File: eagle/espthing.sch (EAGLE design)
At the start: 15 parts, among them IC2 LM1117-3.3, U1 MAX3232

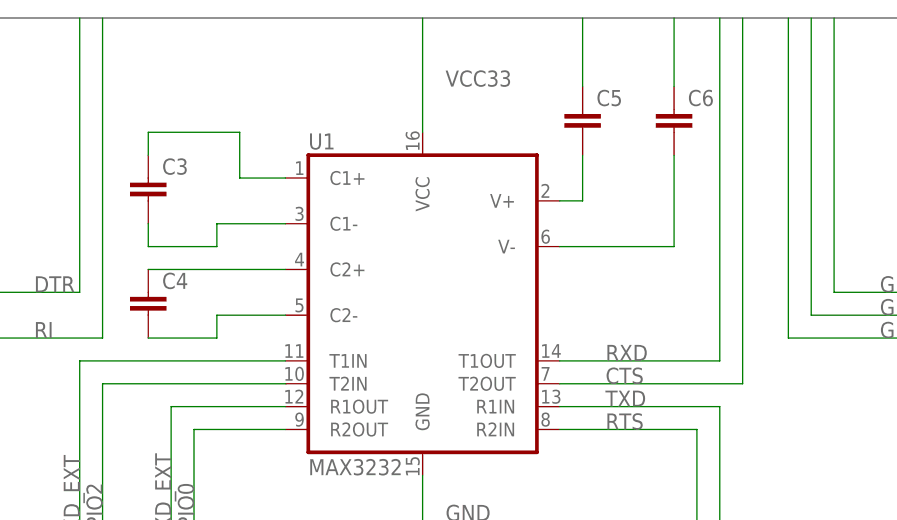
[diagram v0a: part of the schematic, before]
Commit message: added bom
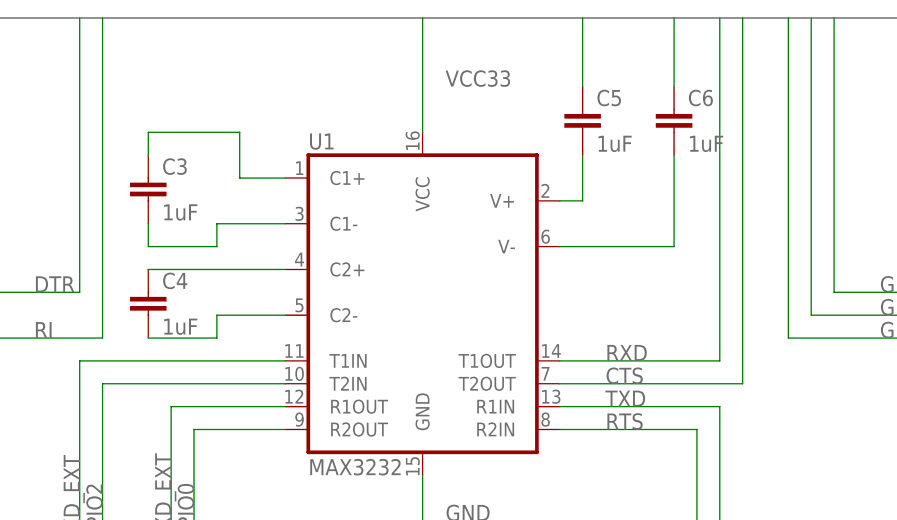
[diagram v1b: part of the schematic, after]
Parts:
- C3, C4, C5, C6: value (none) -> 1uF
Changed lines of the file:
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@@
 <part name="12VPWR" library="SparkFun-Retired" deviceset="JUMPER-2" device="PTH" value="EXT12v"/>
 <part name="X1" library="SparkFun-Retired" library_urn="urn:adsk.eagle:library:533" deviceset="DB25_FEMALE" device="HP" package3d_urn="urn:adsk.eagle:package:41386042/1"/>
-<part name="C3" library="rcl" library_urn="urn:adsk.eagle:library:334" deviceset="C-EU" device="C1206" package3d_urn="urn:adsk.eagle:package:23618/2"/>
-<part name="C4" library="rcl" library_urn="urn:adsk.eagle:library:334" deviceset="C-EU" device="C1206" package3d_urn="urn:adsk.eagle:package:23618/2"/>
-<part name="C5" library="rcl" library_urn="urn:adsk.eagle:library:334" deviceset="C-EU" device="C1206" package3d_urn="urn:adsk.eagle:package:23618/2"/>
-<part name="C6" library="rcl" library_urn="urn:adsk.eagle:library:334" deviceset="C-EU" device="C1206" package3d_urn="urn:adsk.eagle:package:23618/2"/>
+<part name="C3" library="rcl" library_urn="urn:adsk.eagle:library:334" deviceset="C-EU" device="C1206" package3d_urn="urn:adsk.eagle:package:23618/2" value="1uF"/>
+<part name="C4" library="rcl" library_urn="urn:adsk.eagle:library:334" deviceset="C-EU" device="C1206" package3d_urn="urn:adsk.eagle:package:23618/2" value="1uF"/>
+<part name="C5" library="rcl" library_urn="urn:adsk.eagle:library:334" deviceset="C-EU" device="C1206" package3d_urn="urn:adsk.eagle:package:23618/2" value="1uF"/>
+<part name="C6" library="rcl" library_urn="urn:adsk.eagle:library:334" deviceset="C-EU" device="C1206" package3d_urn="urn:adsk.eagle:package:23618/2" value="1uF"/>
 <part name="C89" library="adafruit" library_urn="urn:adsk.eagle:library:420" deviceset="CPOL-US" device="B" package3d_urn="urn:adsk.eagle:package:6240479/1" value="22uF"/>
 <part name="C7" library="microbuilder" deviceset="CAP_CERAMIC" device="1206" value="0.1uF"/>
